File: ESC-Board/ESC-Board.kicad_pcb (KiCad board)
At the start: 2 copper layers, 154 x 62 mm, 26 parts, among them J1 Molex, J2 Molex, J3 XT_60, U1 ESC:Blue_ESC, U2 ESC:Blue_ESC, U3 ESC:Blue_ESC, U4 ESC:Blue_ESC

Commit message: Big PP
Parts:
- D1, D2, D3, D4, F1, F2, F3, F4: moved to B.Cu
- moved D1 0.95 mm to (46.0, 93.0), turned to 90 degrees
- moved D2 0.95 mm to (76.0, 93.0), turned to 90 degrees
- moved D3 0.95 mm to (94.0, 93.0), turned to 90 degrees
- moved D4 0.95 mm to (123.0, 93.0), turned to 90 degrees
- moved F1 0.95 mm to (53.0, 93.0), turned to 270 degrees
- moved F2 0.95 mm to (84.0, 93.0), turned to 270 degrees
- moved F3 0.95 mm to (102.0, 93.0), turned to 270 degrees
- moved F4 0.95 mm to (131.0, 93.0), turned to 270 degrees
- turned J1 to 180 degrees
- turned J2 to 180 degrees

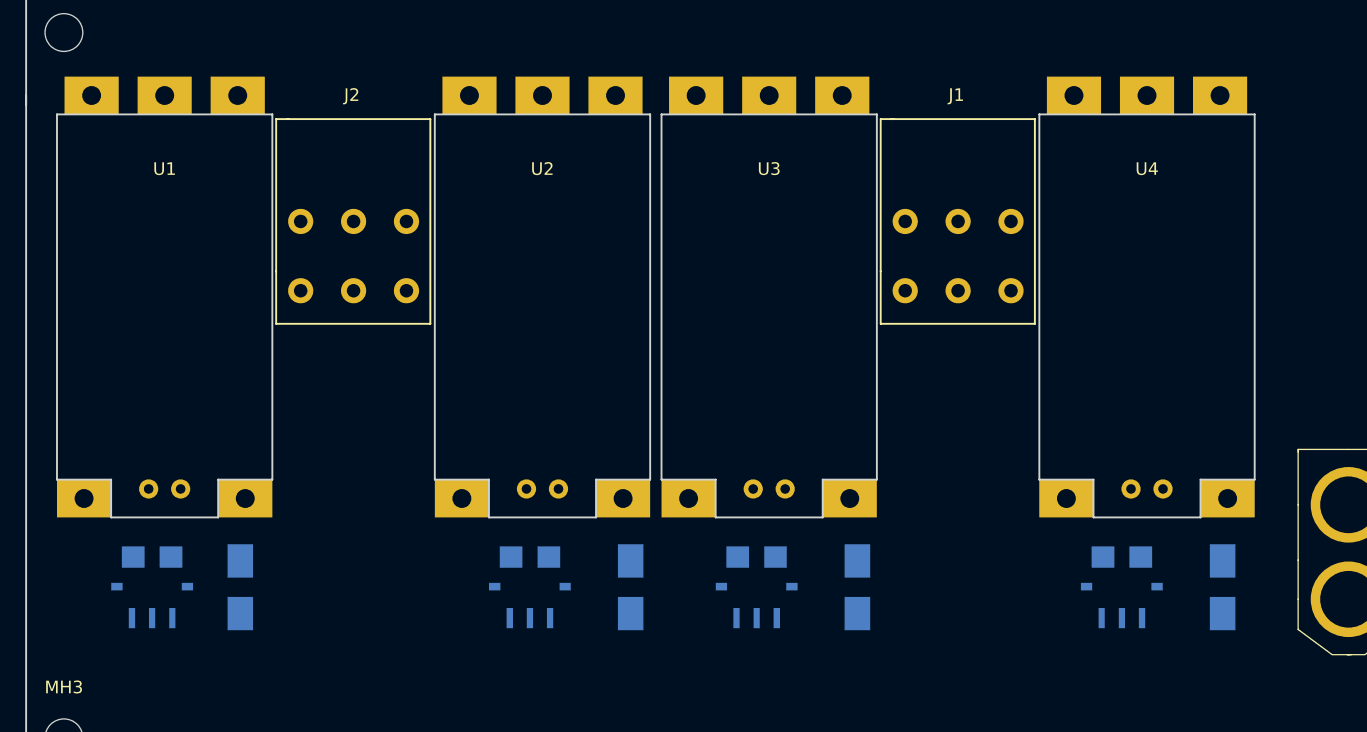
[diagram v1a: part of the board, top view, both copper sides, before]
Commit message: Better footprint
I likey
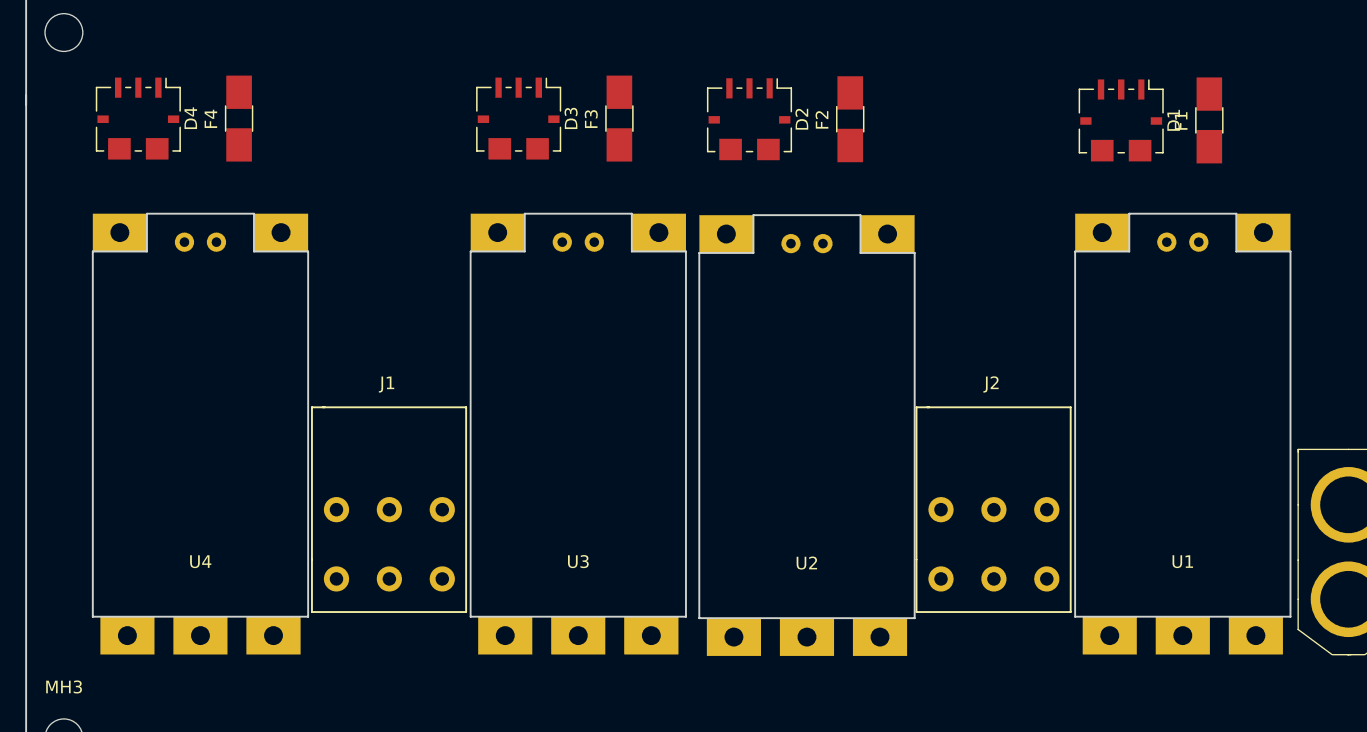
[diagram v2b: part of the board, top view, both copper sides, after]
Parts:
- D1, D2, D3, D4, F1, F2, F3, F4: moved to F.Cu
- moved D4 86.5 mm to (44.9, 55.8), turned to 270 degrees
- moved F4 86.5 mm to (52.9, 55.8), turned to 90 degrees
- moved D1 85.4 mm to (122.9, 56.0), turned to 270 degrees
- moved F1 85.4 mm to (129.9, 56.0), turned to 90 degrees
- moved U1 81.6 mm to (127.8, 80.9), turned to 0 degrees
- moved U4 75.9 mm to (49.8, 80.9), turned to 0 degrees
- moved J2 55.8 mm to (112.8, 86.9)
- moved J1 50.6 mm to (64.8, 86.9)
- moved D3 41.7 mm to (75.1, 55.8), turned to 270 degrees
- moved F3 41.7 mm to (83.1, 55.8), turned to 90 degrees
- moved D2 41.0 mm to (93.4, 55.9), turned to 270 degrees
- moved F2 41.0 mm to (101.4, 55.9), turned to 90 degrees
- moved U2 23.7 mm to (98.0, 81.0), turned to 0 degrees
- moved U3 18.7 mm to (79.8, 80.9), turned to 0 degrees

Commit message: eee
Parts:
- moved J2 12.1 mm to (113.0, 99.0)
- moved J1 12.1 mm to (64.8, 99.0)
- moved U2 2.00 mm to (98.0, 79.0)
- moved U1 1.89 mm to (128.0, 79.0)
- moved U3 1.89 mm to (80.0, 79.0)
- moved U4 1.89 mm to (50.0, 79.0)
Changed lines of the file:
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@@
   )
   (module Blue_ESC:Molex_6pin (layer F.Cu)
-    (at 64.842807 86.884258 180)
+    (at 64.842807 99 180)
     (fp_text reference J1 (at 0.127 10.033 180) (layer F.SilkS)
       (effects (font (size 1 1) (thickness 0.15)))
@@
   )
   (module Blue_ESC:Molex_6pin (layer F.Cu)
-    (at 112.842807 86.884258 180)
+    (at 113 99 180)
     (fp_text reference J2 (at 0.127 10.033 180) (layer F.SilkS)
       (effects (font (size 1 1) (thickness 0.15)))
@@
   )
   (module Blue_ESC:Blue_ESC (layer F.Cu)
-    (at 127.842807 80.884258)
+    (at 128 79)
     (fp_text reference U1 (at 0 10.16) (layer F.SilkS)
       (effects (font (size 1 1) (thickness 0.15)))
@@
   )
   (module Blue_ESC:Blue_ESC (layer F.Cu)
-    (at 98 81)
+    (at 98 79)
     (fp_text reference U2 (at 0 10.16) (layer F.SilkS)
       (effects (font (size 1 1) (thickness 0.15)))
@@
   )
   (module Blue_ESC:Blue_ESC (layer F.Cu)
-    (at 79.842807 80.884258)
+    (at 80 79)
     (fp_text reference U3 (at 0 10.16) (layer F.SilkS)
       (effects (font (size 1 1) (thickness 0.15)))
@@
   )
   (module Blue_ESC:Blue_ESC (layer F.Cu)
-    (at 49.842807 80.884258)
+    (at 50 79)
     (fp_text reference U4 (at 0 10.16) (layer F.SilkS)
       (effects (font (size 1 1) (thickness 0.15)))

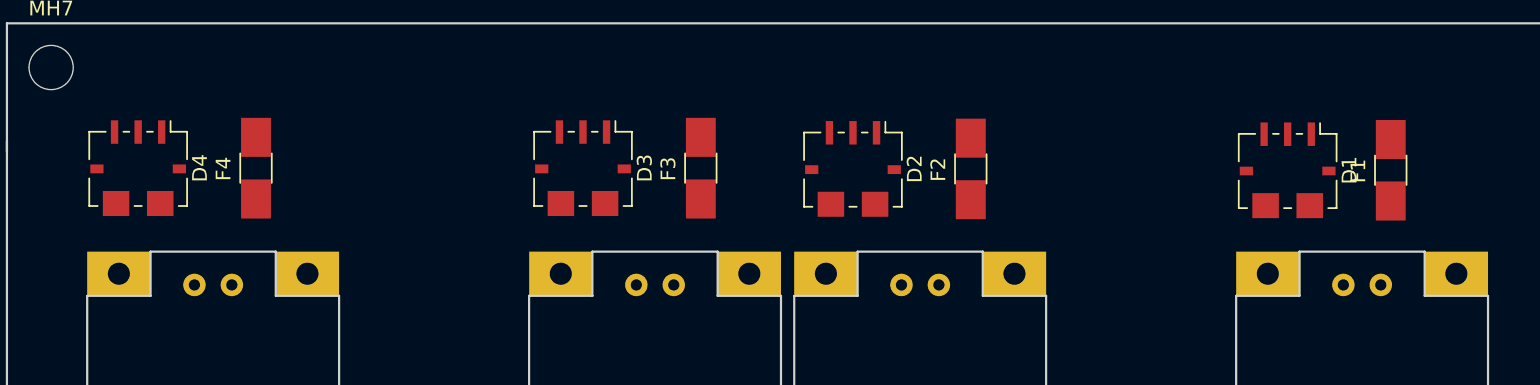
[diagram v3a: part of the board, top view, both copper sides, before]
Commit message: Fixed ESC Pwm lines
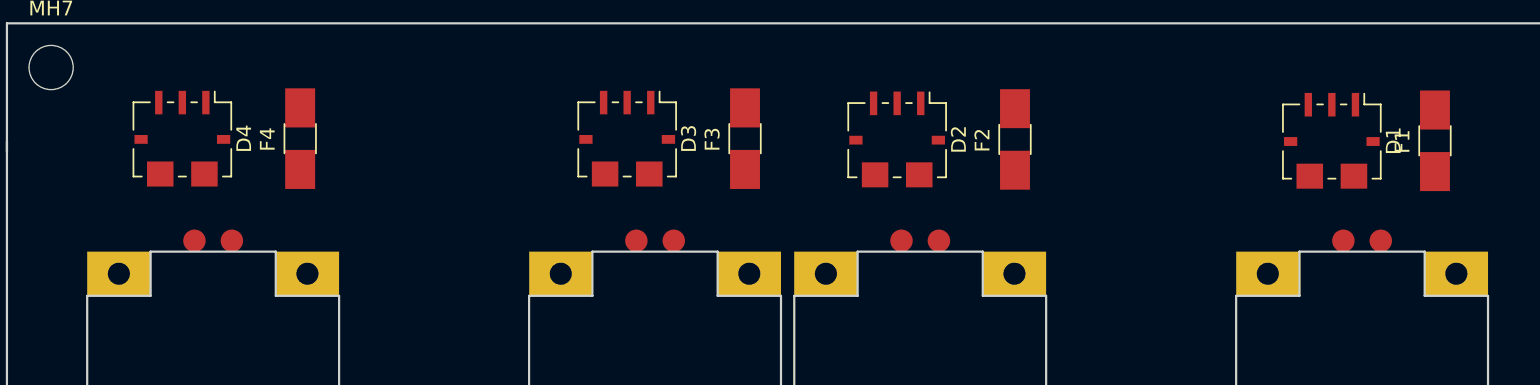
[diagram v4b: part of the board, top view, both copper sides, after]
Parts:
- moved D1 3.61 mm to (125.9, 54.0)
- moved D2 3.61 mm to (96.4, 53.9)
- moved D3 3.61 mm to (78.1, 53.8)
- moved D4 3.61 mm to (47.9, 53.8)
- moved F1 3.61 mm to (132.9, 54.0)
- moved F2 3.61 mm to (104.4, 53.9)
- moved F3 3.61 mm to (86.1, 53.8)
- moved F4 3.61 mm to (55.9, 53.8)

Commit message: More ESC fixes
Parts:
- moved J1 0.16 mm to (65.0, 99.0)
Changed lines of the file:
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@@
     (pad 5 thru_hole rect (at 5.8 16) (size 4.3 3) (drill 1.5) (layers *.Cu *.Mask)
       (net 40 "Net-(J1-Pad1)"))
-    (pad 6 smd circle (at -1.27 -18.2372) (size 1.524 1.524) (layers F.Cu F.Paste F.Mask)
+    (pad 6 smd circle (at -1.27 -18.4912) (size 1.524 1.524) (layers F.Cu F.Paste F.Mask)
       (net 52 PWM_ESC_4))
-    (pad 7 smd circle (at 1.27 -18.2372) (size 1.524 1.524) (layers F.Cu F.Paste F.Mask)
+    (pad 7 smd circle (at 1.27 -18.4912) (size 1.524 1.524) (layers F.Cu F.Paste F.Mask)
       (net 6 GND))
   )
@@
     (pad 5 thru_hole rect (at 5.8 16) (size 4.3 3) (drill 1.5) (layers *.Cu *.Mask)
       (net 46 "Net-(J2-Pad4)"))
-    (pad 6 smd circle (at -1.27 -18.2372) (size 1.524 1.524) (layers F.Cu F.Paste F.Mask)
+    (pad 6 smd circle (at -1.27 -18.4912) (size 1.524 1.524) (layers F.Cu F.Paste F.Mask)
       (net 49 PWM_ESC_1))
-    (pad 7 smd circle (at 1.27 -18.2372) (size 1.524 1.524) (layers F.Cu F.Paste F.Mask)
+    (pad 7 smd circle (at 1.27 -18.4912) (size 1.524 1.524) (layers F.Cu F.Paste F.Mask)
       (net 6 GND))
   )
@@
     (pad 5 thru_hole rect (at 5.8 16) (size 4.3 3) (drill 1.5) (layers *.Cu *.Mask)
       (net 45 "Net-(J2-Pad1)"))
-    (pad 6 smd circle (at -1.27 -18.2372) (size 1.524 1.524) (layers F.Cu F.Paste F.Mask)
+    (pad 6 smd circle (at -1.27 -18.4912) (size 1.524 1.524) (layers F.Cu F.Paste F.Mask)
       (net 50 PWM_ESC_2))
-    (pad 7 smd circle (at 1.27 -18.2372) (size 1.524 1.524) (layers F.Cu F.Paste F.Mask)
+    (pad 7 smd circle (at 1.27 -18.4912) (size 1.524 1.524) (layers F.Cu F.Paste F.Mask)
       (net 6 GND))
   )
@@
     (pad 5 thru_hole rect (at 5.8 16) (size 4.3 3) (drill 1.5) (layers *.Cu *.Mask)
       (net 39 "Net-(J1-Pad4)"))
-    (pad 6 smd circle (at -1.27 -18.2372) (size 1.524 1.524) (layers F.Cu F.Paste F.Mask)
+    (pad 6 smd circle (at -1.27 -18.4912) (size 1.524 1.524) (layers F.Cu F.Paste F.Mask)
       (net 51 PWM_ESC_3))
-    (pad 7 smd circle (at 1.27 -18.2372) (size 1.524 1.524) (layers F.Cu F.Paste F.Mask)
+    (pad 7 smd circle (at 1.27 -18.4912) (size 1.524 1.524) (layers F.Cu F.Paste F.Mask)
       (net 6 GND))
   )
@@
   )
   (module Blue_ESC:Molex_6pin (layer F.Cu)
-    (at 64.842807 99 180)
+    (at 65 99 180)
     (fp_text reference J1 (at 0.127 10.033 180) (layer F.SilkS)
       (effects (font (size 1 1) (thickness 0.15)))
